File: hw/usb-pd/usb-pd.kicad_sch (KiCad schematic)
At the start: 0 parts

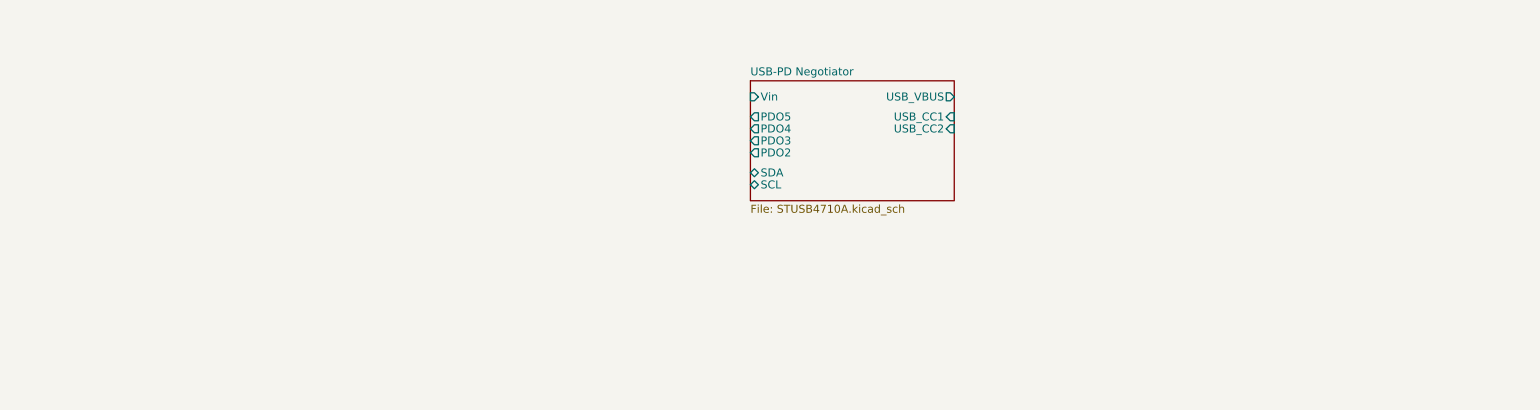
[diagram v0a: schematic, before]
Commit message: Schematic complete, calculation of components required for MAX25240
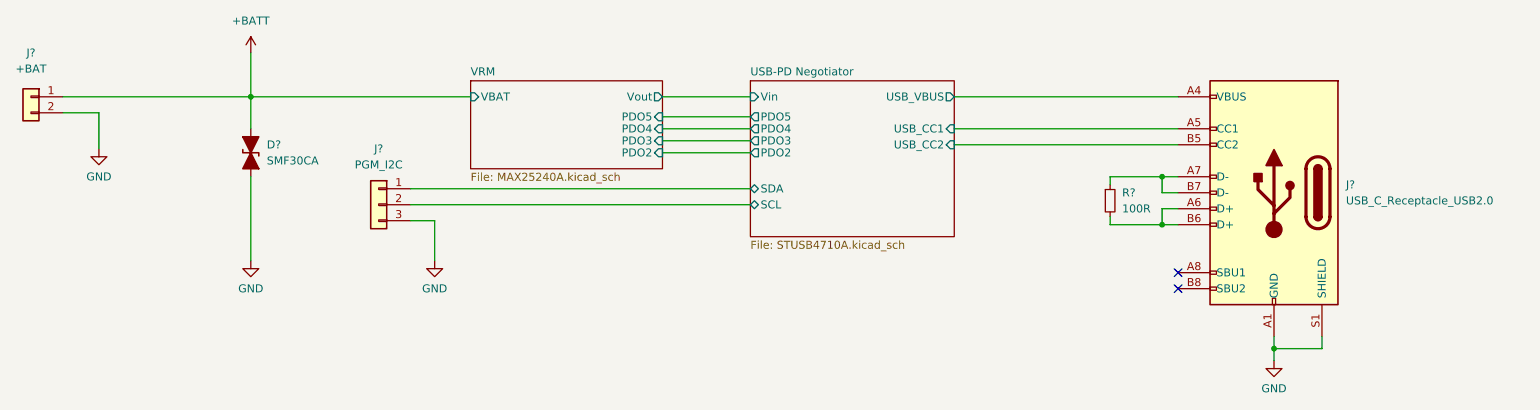
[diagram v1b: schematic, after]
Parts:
- added D?: SMF30CA, Diode_SMD:D_SOD-123, symbol Device:D_TVS_Filled
- added J?: +BAT, Connector_JST:JST_PH_B2B-PH-K_1x02_P2.00mm_Vertical, symbol Connector_Generic:Conn_01x02
- added J?: USB_C_Receptacle_USB2.0, footprints:USB4105-GF-A, symbol Connector:USB_C_Receptacle_USB2.0
- added J?: PGM_I2C, Connector_PinHeader_2.54mm:PinHeader_1x03_P2.54mm_Vertical, symbol Connector_Generic:Conn_01x03
- added R?: 100R, Resistor_SMD:R_0603_1608Metric_Pad0.98x0.95mm_HandSolder, symbol Device:R_Small
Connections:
- net USB-PD Negotiator/SCL: now also J?.2 (Pin_2)
- net USB-PD Negotiator/SDA: now also J?.1 (Pin_1)
- net USB-PD Negotiator/USB_CC1: now also J?.A5 (CC1)
- net USB-PD Negotiator/USB_CC2: now also J?.B5 (CC2)
- net USB-PD Negotiator/USB_VBUS: now also J?.A4 (VBUS), J?.A9 (VBUS), J?.B4 (VBUS), J?.B9 (VBUS)
- new net: J?.A6 (D+), J?.B6 (D+), R?.2
- new net: J?.A7 (D-), J?.B7 (D-), R?.1
- new net +BATT: D?.2 (A2), J?.1 (Pin_1)
- new net GND: D?.1 (A1), J?.2 (Pin_2), J?.3 (Pin_3), J?.A1 (GND), J?.A12 (GND), J?.B1 (GND), J?.B12 (GND), J?.S1 (SHIELD)
- no-connect marks 0 -> 2
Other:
- added sheet VRM (MAX25240A.kicad_sch)

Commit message: Preliminary PCB layout, calculated compensation filter and feedback network for MAX25240
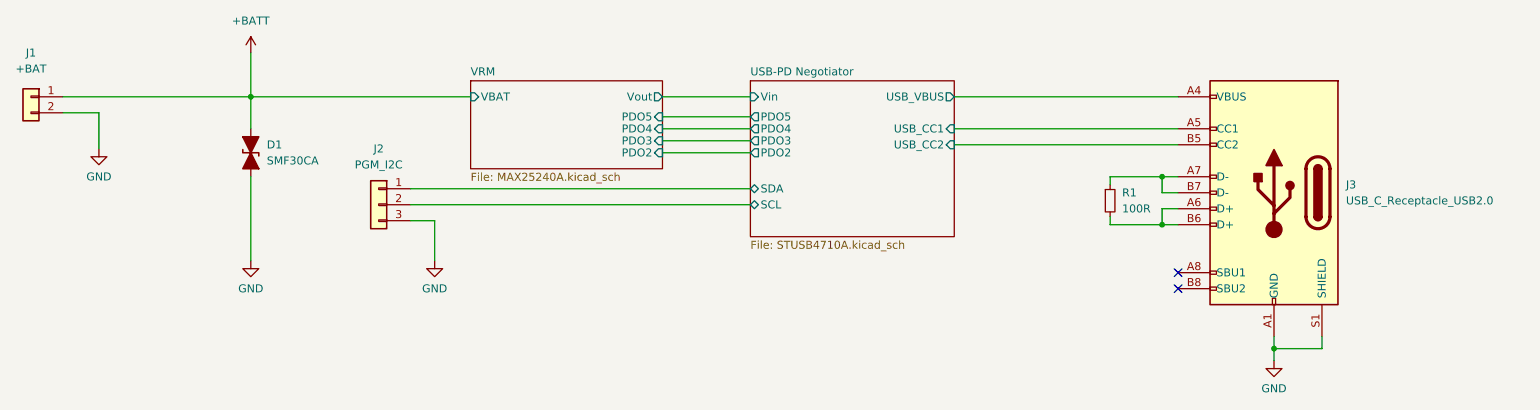
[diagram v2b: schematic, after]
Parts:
- gave numbers to parts that had none: 5
